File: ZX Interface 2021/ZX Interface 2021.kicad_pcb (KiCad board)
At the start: 2 copper layers, 87.6 x 99.9 mm, 54 parts, among them J1 PORT 1, J2 PORT 2, J3 SWAP_ROMS, J4 Extended Cartridge Port, J5 JOYSTICK_EN, M1 Mounting, M2 Mounting, M3 Mounting, M4 Mounting, M5 Mounting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

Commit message: Cartridge pins were mirrored, still need to change cartridges
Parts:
- removed J3: SWAP_ROMS, Connector_PinHeader_2.54mm:PinHeader_2x02_P2.54mm_Vertical
- added D11: PWR, LED_THT:LED_D5.0mm, F.Cu at (184.8, 57.8)
- added R14: 330, Resistor_THT:R_Axial_DIN0207_L6.3mm_D2.5mm_P10.16mm_Horizontal, F.Cu at (162.6, 88.3)
- moved C5 1.83 mm to (105.7, 129.3), turned to 90 degrees
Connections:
- U7 pad 14: Net-(J3-Pad4) -> /~ROM_1
- U7 pad 15: Net-(J3-Pad1) -> /~ROM_0
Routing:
- net VCC: track 336.4 -> 381.0 mm
- net Net-(D11-Pad1): track 0.00 -> 38.5 mm, vias 0 -> 1
- net Net-(J3-Pad1): track 38.0 -> 0.00 mm, vias 2 -> 0
- net Net-(J3-Pad4): track 30.3 -> 0.00 mm, vias 2 -> 0
- net /~ROM_0: track 11.1 -> 33.6 mm
- net /~ROM_1: track 8.67 -> 19.1 mm, vias 0 -> 1
- net /BA14: track 14.1 -> 21.3 mm, vias 1 -> 2
- net /A9: track 77.9 -> 71.2 mm, vias 3 -> 1
- net /D3: track 154.0 -> 160.3 mm
- net /~ROM_2: track 26.6 -> 20.4 mm, vias 3 -> 2
- net /A8: track 71.1 -> 65.0 mm, vias 2 -> 1
- net /D0: track 124.1 -> 118.4 mm
- net /A14: track 66.0 -> 60.5 mm
- net /A2: track 45.6 -> 51.1 mm
- net /A11: track 134.2 -> 139.7 mm
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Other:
- board text removed: "ROM 0"
- board text removed: "ROM 1"
- board text removed: "SWAP_ROMS"

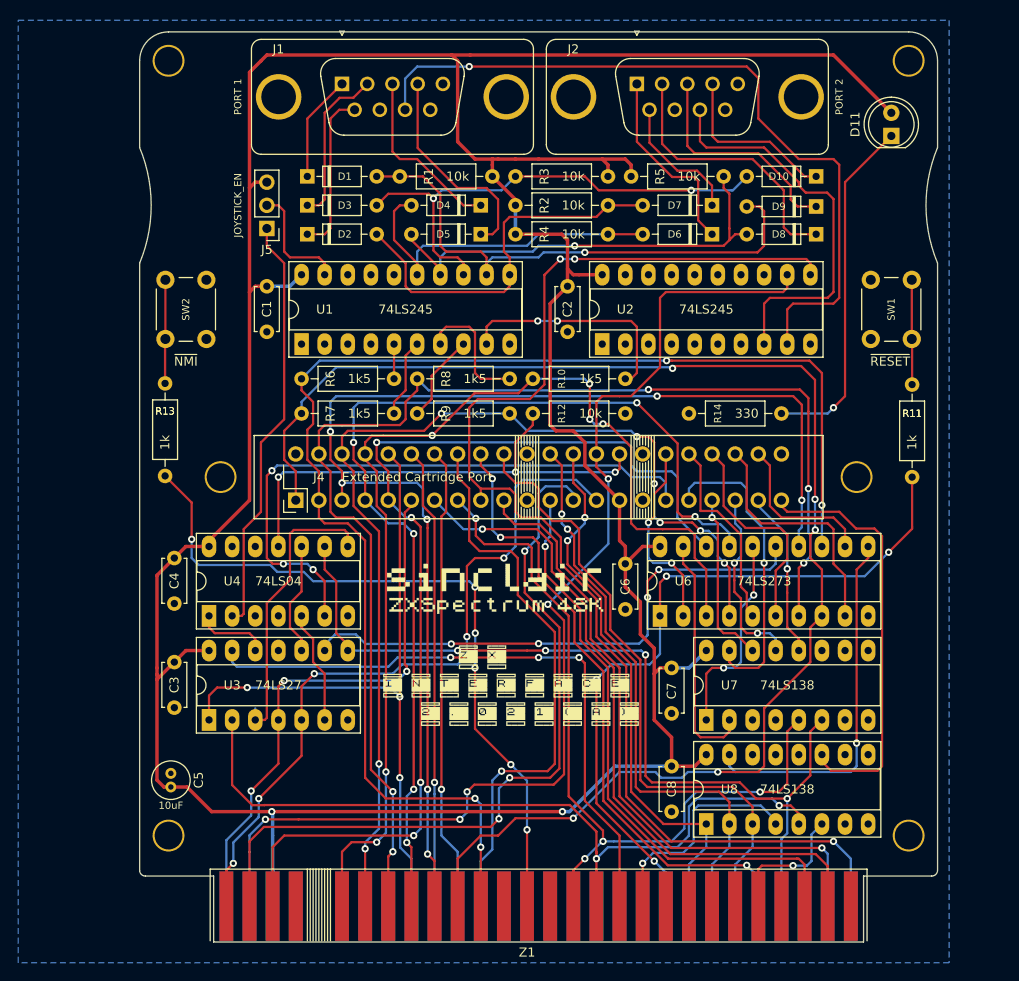
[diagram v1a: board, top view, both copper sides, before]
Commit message: Made 74ls245 open collector instead of using resistors
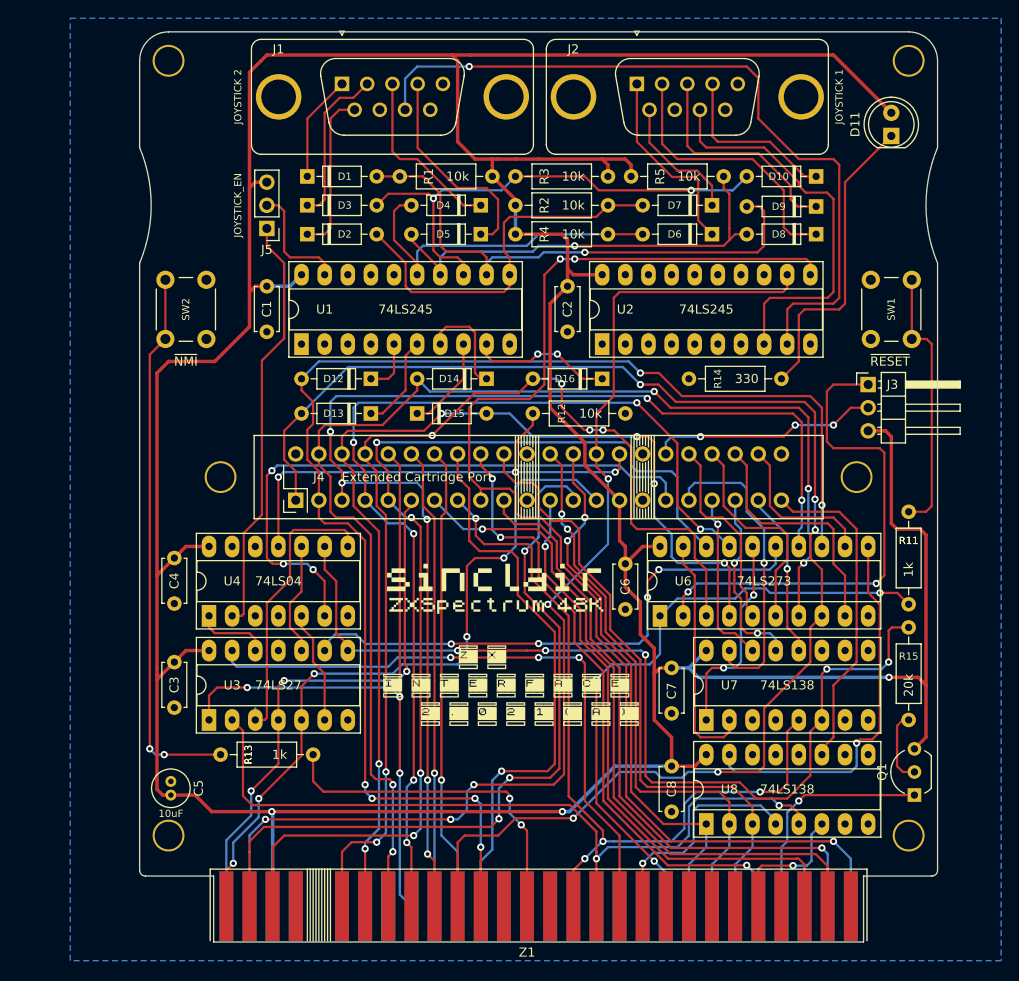
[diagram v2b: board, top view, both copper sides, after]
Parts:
- removed R10, R6, R7, R8, R9: 1k5, Resistor_THT:R_Axial_DIN0207_L6.3mm_D2.5mm_P10.16mm_Horizontal
- added D12: 1n4148, 1n4148:D_DO-35_SOD27_P7.62mm_Horizontal, F.Cu at (127.6, 84.5)
- added D13: 1n4148, 1n4148:D_DO-35_SOD27_P7.62mm_Horizontal, F.Cu at (127.6, 88.3)
- added D14: 1n4148, 1n4148:D_DO-35_SOD27_P7.62mm_Horizontal, F.Cu at (140.3, 84.5)
- added D15: 1n4148, 1n4148:D_DO-35_SOD27_P7.62mm_Horizontal, F.Cu at (132.7, 88.3)
- added D16: 1n4148, 1n4148:D_DO-35_SOD27_P7.62mm_Horizontal, F.Cu at (153.0, 84.5)
- added J3: BA14_HI, Connector_PinHeader_2.54mm:PinHeader_1x03_P2.54mm_Horizontal, F.Cu at (182.2, 85.1)
- added Q1: 2N3904, Package_TO_SOT_THT:TO-92_Inline_Wide, F.Cu at (187.3, 130.2)
- added R15: 20k, Resistor_THT:R_Axial_DIN0207_L6.3mm_D2.5mm_P10.16mm_Horizontal, F.Cu at (186.7, 121.9)
- J1: value PORT 1 -> JOYSTICK 2
- J2: value PORT 2 -> JOYSTICK 1
- moved R13 41.2 mm to (111.1, 125.7), turned to 0 degrees
- moved R11 14.0 mm to (186.7, 99.1)
- moved R14 3.81 mm to (162.6, 84.5)
- moved C5 0.89 mm to (105.7, 130.2)
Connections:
- U3 pad 8: /~ROMCS -> Net-(R15-Pad2)
- U4 pad 9: /~ROMCS -> Net-(R15-Pad2)
- U6 pad 2: /BA14 -> Net-(J3-Pad1)
- U7 pad 6: /~ROMCS -> Net-(R15-Pad2)
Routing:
- net Net-(R15-Pad2): track 0.00 -> 104.2 mm, vias 0 -> 5
- net VCC: track 381.0 -> 456.4 mm, vias 2 -> 3
- net /~ROMCS: track 97.6 -> 25.3 mm, vias 4 -> 1
- net Net-(J3-Pad1): track 0.00 -> 55.8 mm, vias 0 -> 2
- net Net-(R13-Pad1): track 11.4 -> 60.5 mm, vias 0 -> 2
- net /~NMI: track 80.1 -> 38.1 mm, vias 6 -> 2
- net Net-(R11-Pad1): track 11.5 -> 29.5 mm
- net /~RESET: track 81.7 -> 70.2 mm, vias 4 -> 3
- net OUT_63: track 46.3 -> 35.9 mm
- net Net-(D16-Pad1): track 25.6 -> 15.7 mm
- net Net-(Q1-Pad2): track 0.00 -> 8.15 mm
- net Net-(D11-Pad1): track 38.5 -> 33.9 mm, vias 1 -> 0
- net /BA14: track 21.3 -> 25.1 mm, vias 2 -> 3
- net Net-(D14-Pad1): track 14.1 -> 11.6 mm
- net Net-(D12-Pad1): track 3.81 -> 5.98 mm
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
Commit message: Cleanup
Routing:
- net Net-(R11-Pad1): track 29.5 -> 25.6 mm
- net Net-(J3-Pad1): track 55.8 -> 53.0 mm
- net /D5: track 133.8 -> 131.2 mm
- net /D6: track 111.4 -> 109.2 mm
- net /D3: track 158.3 -> 159.5 mm
- net /D0: track 117.6 -> 118.8 mm, vias 6 -> 5
- net Net-(D15-Pad1): track 10.5 -> 11.5 mm
- net /D2: track 138.8 -> 138.1 mm
- net Net-(D13-Pad1): track 10.5 -> 9.72 mm
- net /~RESET: track 70.2 -> 70.8 mm

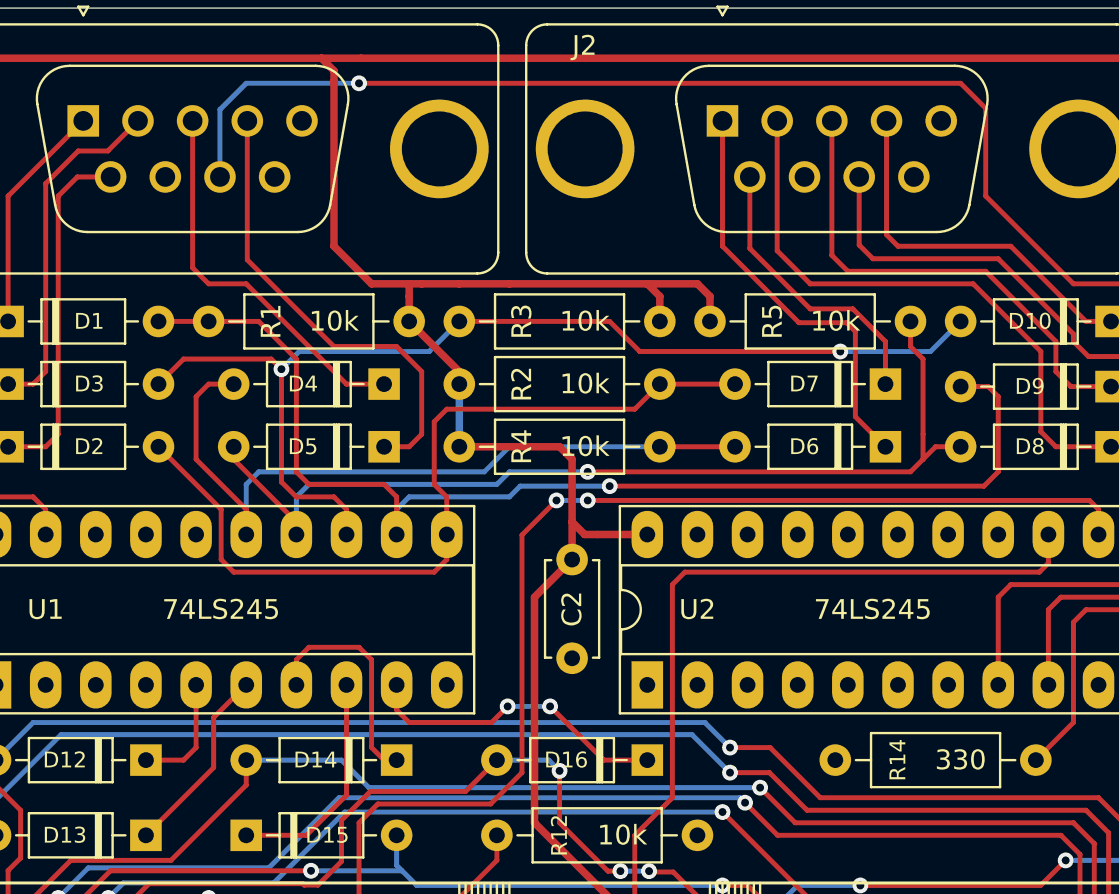
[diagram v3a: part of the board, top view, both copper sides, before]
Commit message: unscrambled joystick pins
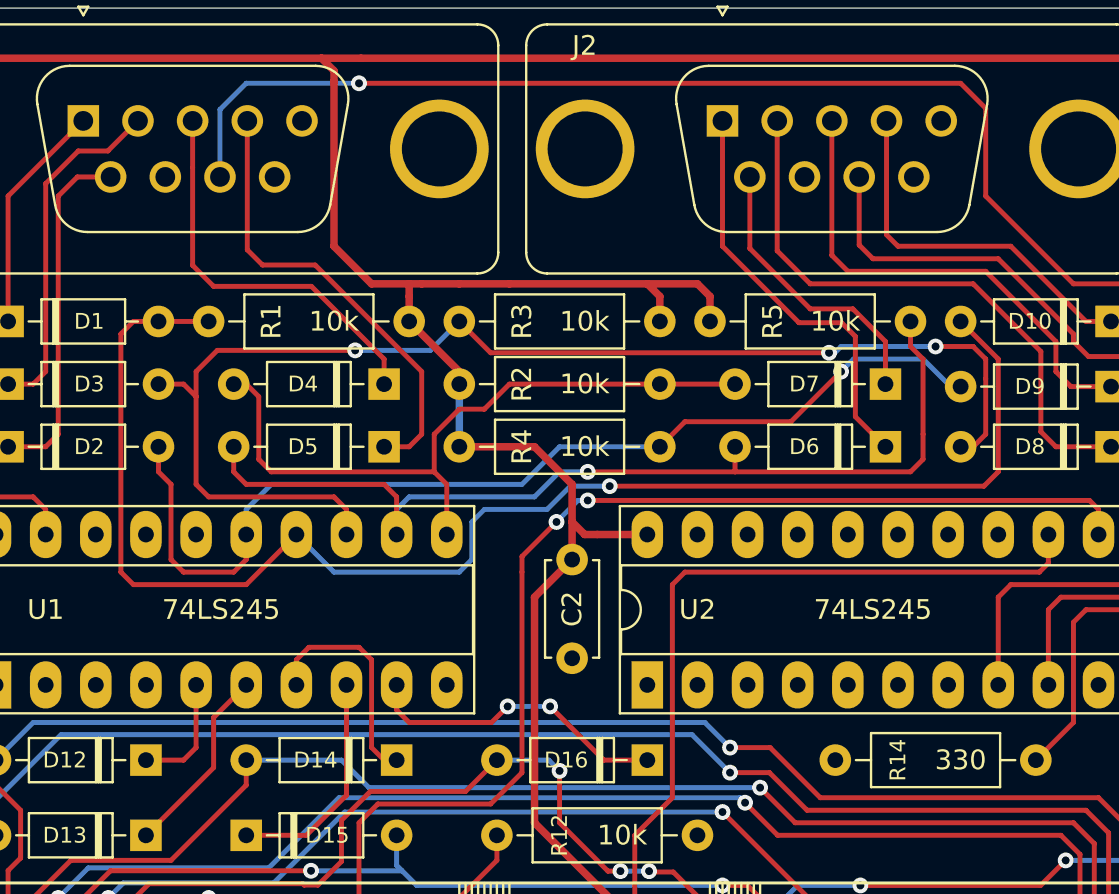
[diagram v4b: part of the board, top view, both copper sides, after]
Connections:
- D10 pad 2: Net-(D10-Pad2) -> Net-(D1-Pad2)
- D3 pad 2: Net-(D10-Pad2) -> Net-(D3-Pad2)
- D6 pad 2: Net-(D4-Pad2) -> Net-(D5-Pad2)
- D7 pad 2: Net-(D2-Pad2) -> Net-(D4-Pad2)
- D8 pad 2: Net-(D5-Pad2) -> Net-(D3-Pad2)
- D9 pad 2: Net-(D1-Pad2) -> Net-(D2-Pad2)
- R2 pad 2: Net-(D2-Pad2) -> Net-(D4-Pad2)
- R3 pad 2: Net-(D10-Pad2) -> Net-(D3-Pad2)
- R4 pad 2: Net-(D4-Pad2) -> Net-(D2-Pad2)
- U1 pad 11: Net-(D2-Pad2) -> Net-(D4-Pad2)
- U1 pad 12: Net-(D1-Pad2) -> Net-(D5-Pad2)
- U1 pad 13: Net-(D10-Pad2) -> Net-(D3-Pad2)
- U1 pad 14: Net-(D5-Pad2) -> Net-(D1-Pad2)
- U1 pad 15: Net-(D4-Pad2) -> Net-(D2-Pad2)
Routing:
- net Net-(D3-Pad2): track 0.00 -> 64.8 mm, vias 0 -> 3
- net Net-(D10-Pad2): track 54.5 -> 0.00 mm, vias 2 -> 0
- net Net-(D1-Pad2): track 59.5 -> 75.0 mm
- net Net-(D2-Pad2): track 42.3 -> 52.8 mm, vias 0 -> 1
- net Net-(D4-Pad2): track 38.3 -> 35.5 mm
- net VCC: track 456.4 -> 455.6 mm
- net Net-(D4-Pad1): track 19.6 -> 20.3 mm
- net /A11: track 139.7 -> 139.0 mm

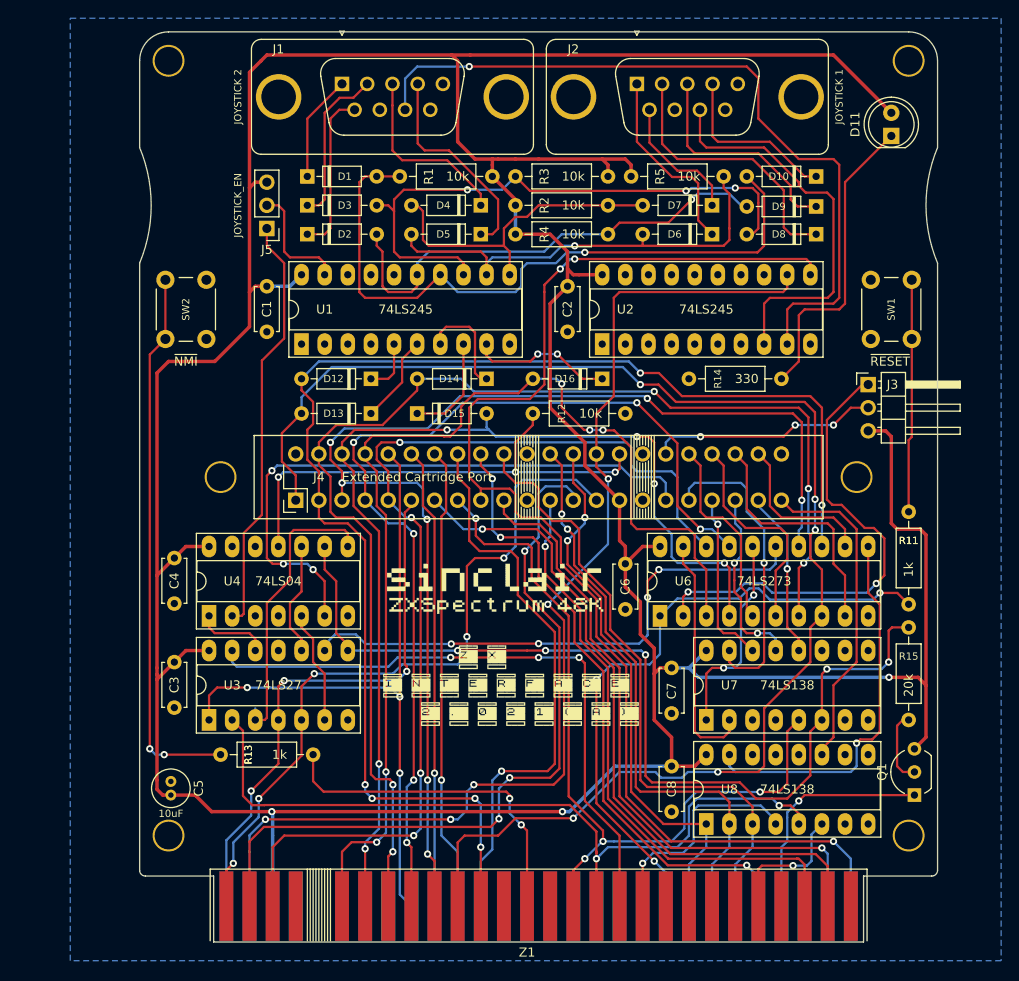
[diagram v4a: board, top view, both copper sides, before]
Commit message: Tweaked interface title
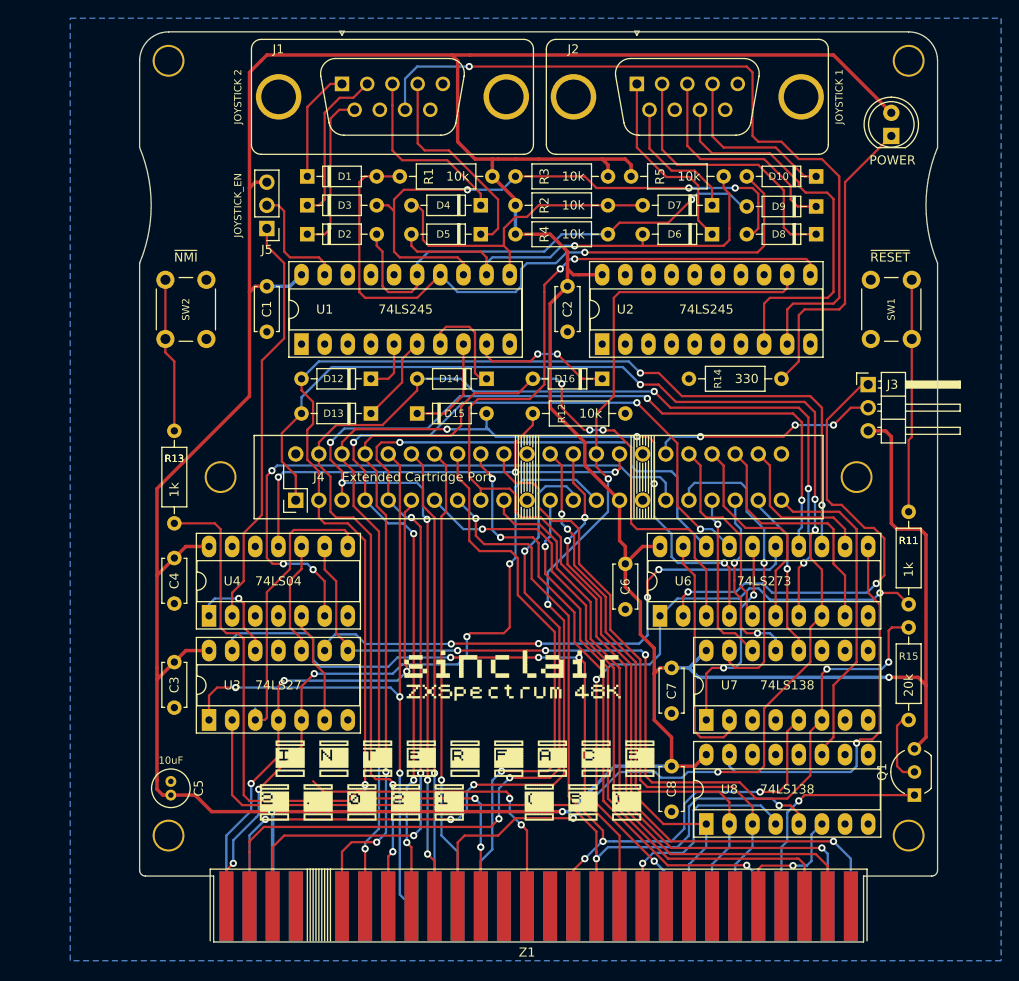
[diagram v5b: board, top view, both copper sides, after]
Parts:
- D11: value PWR -> POWER
- moved R13 35.9 mm to (106.0, 90.2), turned to 270 degrees
- moved sinclair_title 14.5 mm to (115.6, 119.4)
- moved sinclair_title 9.71 mm to (130.8, 114.3)
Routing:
- net /~NMI: track 38.1 -> 85.3 mm
- net Net-(R13-Pad1): track 60.5 -> 17.0 mm, vias 2 -> 0
- net Net-(U3-Pad12): track 8.15 -> 11.3 mm, vias 0 -> 1
- net VCC: track 455.6 -> 452.6 mm
- net /~RD: track 69.2 -> 72.1 mm
- net Net-(J1-Pad8): track 83.4 -> 84.1 mm
- net Net-(D1-Pad1): track 12.4 -> 13.1 mm
- net /~IORQ: track 86.3 -> 86.9 mm
- net Net-(J5-Pad1): track 46.3 -> 45.7 mm
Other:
- board text removed: "ATARI PORT 1"
- board text removed: "ATARI PORT 2"

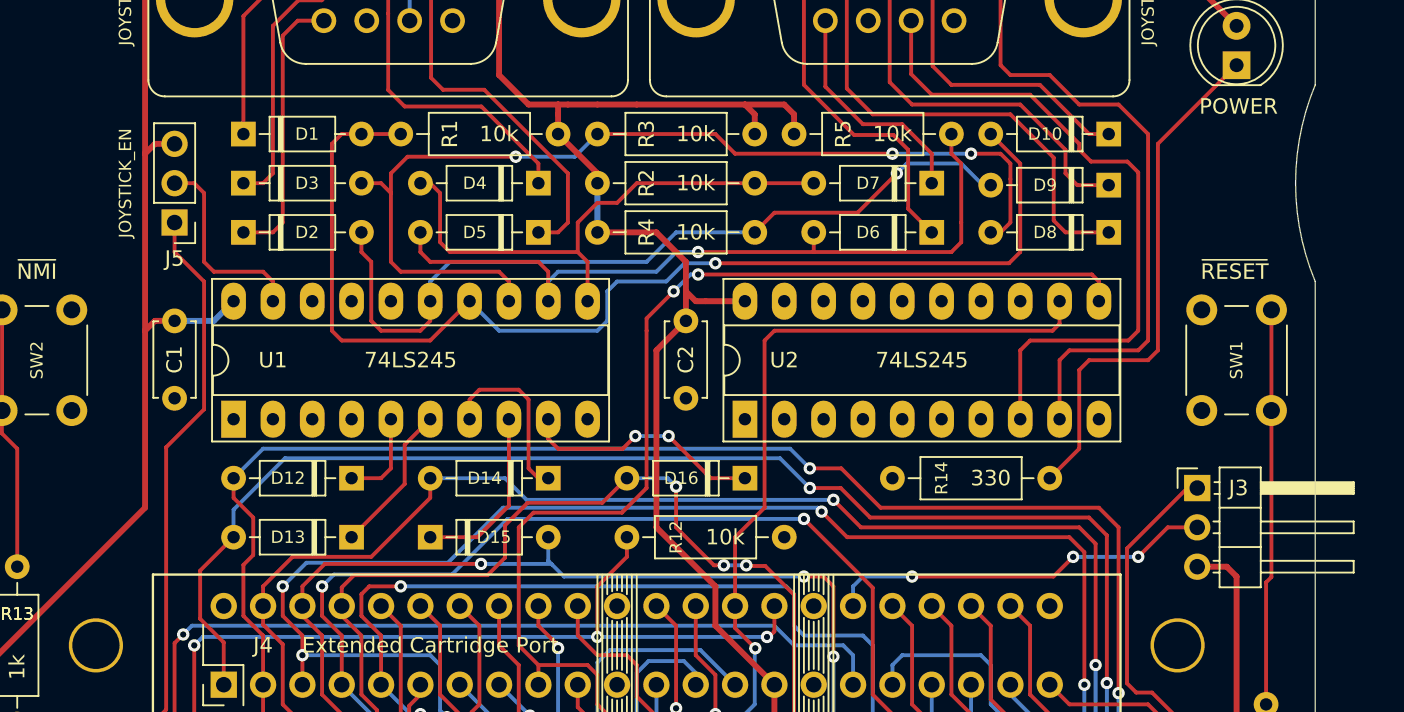
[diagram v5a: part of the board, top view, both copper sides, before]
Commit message: Silkscreen tweaks
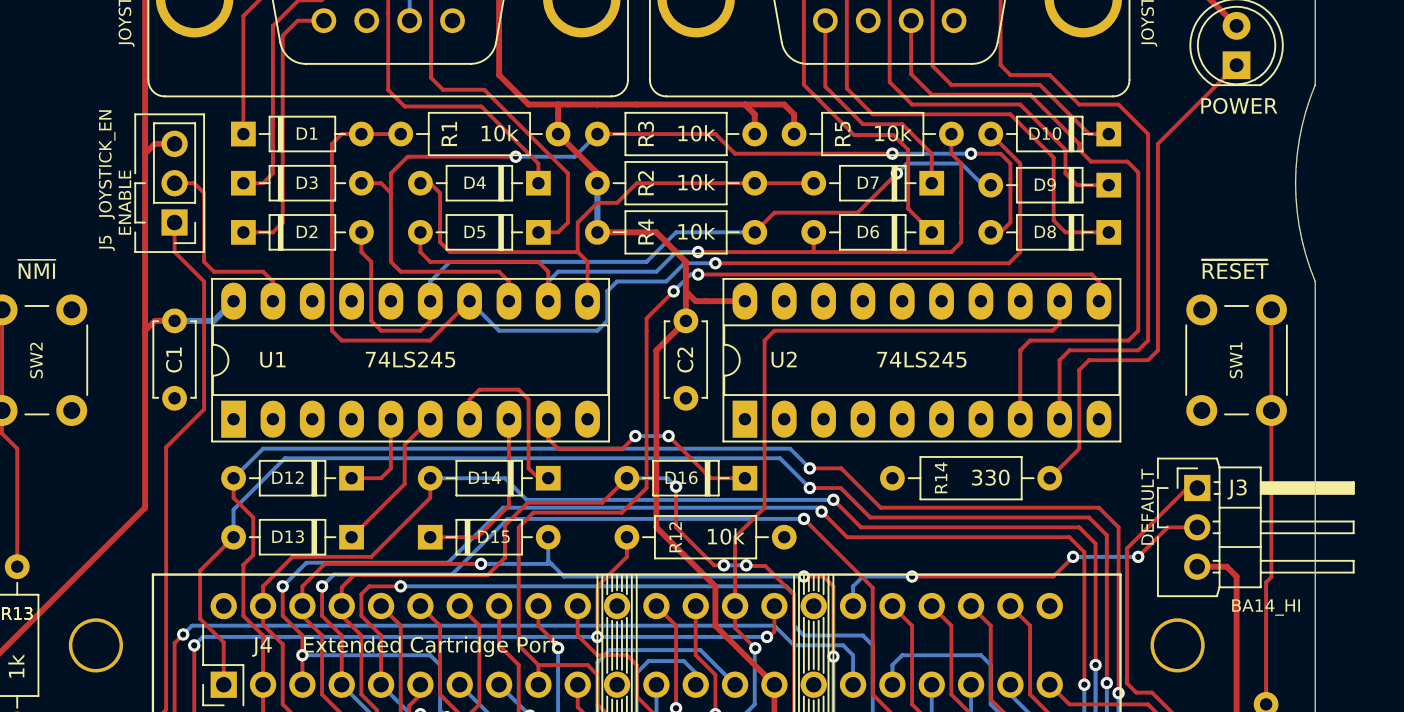
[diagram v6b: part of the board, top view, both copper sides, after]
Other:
- board text added: "DEFAULT"
- board text added: "FORCE BA14 HIGH (WHEN BOOT NOT POSSIBLE)"
